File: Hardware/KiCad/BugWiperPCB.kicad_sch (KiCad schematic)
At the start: 0 parts

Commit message: update KiCAD files
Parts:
- added J2: Conn_01x06, symbol Connector_Generic:Conn_01x06
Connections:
- new net +3V3: J2.2 (Pin_2)
- new net EN_C1: J2.4 (Pin_4)
- new net EN_C2: J2.3 (Pin_3)
- new net GND: J2.5 (Pin_5)
- new net Motor+: J2.1 (Pin_1)
- new net Motor-: J2.6 (Pin_6)
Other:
- sheet ESP32-S3 ports: added ADC_VBat, Encoder_C1, Encoder_C2, M_IHN2, M_IN1, M_IN2, M_INH1, M_IS1, M_IS2; removed none
- sheet Power ports: added +3V3, +VBat, -VBat, ADC_VBat, GND, M_IN1, M_IN2, M_INH1, M_INH2, M_IS1, M_IS2, Motor+, Motor-; removed none
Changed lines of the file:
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@@
 (kicad_sch (version 20230121) (generator eeschema)
   (paper "A4")
-  (sheet (at 142.24 73.66) (size 33.02 21.59) (fields_autoplaced)
+  (wire (pts (xy 214.63 140.97) (xy 220.98 140.97))
+    (stroke (width 0) (type default))
+  )
+  (wire (pts (xy 180.34 73.66) (xy 187.96 73.66))
+    (stroke (width 0) (type default))
+  )
+  (wire (pts (xy 116.84 76.2) (xy 142.24 76.2))
+    (stroke (width 0) (type default))
+  )
+  (wire (pts (xy 214.63 138.43) (xy 220.98 138.43))
+    (stroke (width 0) (type default))
+  )
+  (wire (pts (xy 116.84 64.77) (xy 142.24 64.77))
+    (stroke (width 0) (type default))
+  )
+  (wire (pts (xy 214.63 143.51) (xy 220.98 143.51))
+    (stroke (width 0) (type default))
+  )
+  (wire (pts (xy 180.34 80.01) (xy 187.96 80.01))
+    (stroke (width 0) (type default))
+  )
+  (wire (pts (xy 214.63 151.13) (xy 220.98 151.13))
+    (stroke (width 0) (type default))
+  )
+  (wire (pts (xy 116.84 54.61) (xy 142.24 54.61))
+    (stroke (width 0) (type default))
+  )
+  (wire (pts (xy 72.39 74.93) (xy 76.2 74.93))
+    (stroke (width 0) (type default))
+  )
+  (wire (pts (xy 214.63 148.59) (xy 220.98 148.59))
+    (stroke (width 0) (type default))
+  )
+  (wire (pts (xy 116.84 99.06) (xy 142.24 99.06))
+    (stroke (width 0) (type default))
+  )
+  (wire (pts (xy 116.84 73.66) (xy 142.24 73.66))
+    (stroke (width 0) (type default))
+  )
+  (wire (pts (xy 116.84 50.8) (xy 142.24 50.8))
+    (stroke (width 0) (type default))
+  )
+  (wire (pts (xy 72.39 71.12) (xy 76.2 71.12))
+    (stroke (width 0) (type default))
+  )
+  (wire (pts (xy 214.63 146.05) (xy 220.98 146.05))
+    (stroke (width 0) (type default))
+  )
+  (wire (pts (xy 116.84 67.31) (xy 142.24 67.31))
+    (stroke (width 0) (type default))
+  )
+  (global_label "EN_C1" (shape input) (at 214.63 146.05 180) (fields_autoplaced)
+    (effects (font (size 1.27 1.27)) (justify right))
+    (property "Intersheetrefs" "${INTERSHEET_REFS}" (at 205.7182 146.05 0)
+      (effects (font (size 1.27 1.27)) (justify right) hide)
+    )
+  )
+  (global_label "Motor-" (shape input) (at 214.63 151.13 180) (fields_autoplaced)
+    (effects (font (size 1.27 1.27)) (justify right))
+    (property "Intersheetrefs" "${INTERSHEET_REFS}" (at 204.8111 151.13 0)
+      (effects (font (size 1.27 1.27)) (justify right) hide)
+    )
+  )
+  (global_label "+3V3" (shape input) (at 214.63 140.97 180) (fields_autoplaced)
+    (effects (font (size 1.27 1.27)) (justify right))
+    (property "Intersheetrefs" "${INTERSHEET_REFS}" (at 206.5648 140.97 0)
+      (effects (font (size 1.27 1.27)) (justify right) hide)
+    )
+  )
+  (global_label "Motor+" (shape input) (at 214.63 138.43 180) (fields_autoplaced)
+    (effects (font (size 1.27 1.27)) (justify right))
+    (property "Intersheetrefs" "${INTERSHEET_REFS}" (at 204.8111 138.43 0)
+      (effects (font (size 1.27 1.27)) (justify right) hide)
+    )
+  )
+  (global_label "GND" (shape input) (at 214.63 148.59 180) (fields_autoplaced)
+    (effects (font (size 1.27 1.27)) (justify right))
+    (property "Intersheetrefs" "${INTERSHEET_REFS}" (at 207.7743 148.59 0)
+      (effects (font (size 1.27 1.27)) (justify right) hide)
+    )
+  )
+  (global_label "Motor+" (shape input) (at 187.96 73.66 0) (fields_autoplaced)
+    (effects (font (size 1.27 1.27)) (justify left))
+    (property "Intersheetrefs" "${INTERSHEET_REFS}" (at 197.7789 73.66 0)
+      (effects (font (size 1.27 1.27)) (justify left) hide)
+    )
+  )
+  (global_label "Motor-" (shape input) (at 187.96 80.01 0) (fields_autoplaced)
+    (effects (font (size 1.27 1.27)) (justify left))
+    (property "Intersheetrefs" "${INTERSHEET_REFS}" (at 197.7789 80.01 0)
+      (effects (font (size 1.27 1.27)) (justify left) hide)
+    )
+  )
+  (global_label "EN_C2" (shape input) (at 72.39 74.93 180) (fields_autoplaced)
+    (effects (font (size 1.27 1.27)) (justify right))
+    (property "Intersheetrefs" "${INTERSHEET_REFS}" (at 63.4782 74.93 0)
+      (effects (font (size 1.27 1.27)) (justify right) hide)
+    )
+  )
+  (global_label "EN_C2" (shape input) (at 214.63 143.51 180) (fields_autoplaced)
+    (effects (font (size 1.27 1.27)) (justify right))
+    (property "Intersheetrefs" "${INTERSHEET_REFS}" (at 205.7182 143.51 0)
+      (effects (font (size 1.27 1.27)) (justify right) hide)
+    )
+  )
+  (global_label "EN_C1" (shape input) (at 72.39 71.12 180) (fields_autoplaced)
+    (effects (font (size 1.27 1.27)) (justify right))
+    (property "Intersheetrefs" "${INTERSHEET_REFS}" (at 63.4782 71.12 0)
+      (effects (font (size 1.27 1.27)) (justify right) hide)
+    )
+  )
+  (symbol (lib_id "Connector_Generic:Conn_01x06") (at 226.06 143.51 0) (unit 1)
+    (in_bom yes) (on_board yes) (dnp no) (fields_autoplaced)
+    (property "Reference" "J2" (at 228.6 143.51 0)
+      (effects (font (size 1.27 1.27)) (justify left))
+    )
+    (property "Value" "Conn_01x06" (at 228.6 146.05 0)
+      (effects (font (size 1.27 1.27)) (justify left))
+    )
+    (property "Footprint" "" (at 226.06 143.51 0)
+      (effects (font (size 1.27 1.27)) hide)
+    )
+    (property "Datasheet" "~" (at 226.06 143.51 0)
+      (effects (font (size 1.27 1.27)) hide)
+    )
+    (pin "2")
+    (pin "1")
+    (pin "6")
+    (pin "4")
+    (pin "5")
+    (pin "3")
+    (instances
+      (project "BugWiperPCB"
+        (path "/d31a15bd-db02-4d4c-9593-17c596d3182c"
+          (reference "J2") (unit 1)
+        )
+      )
+    )
+  )
+  (sheet (at 142.24 46.99) (size 38.1 57.15) (fields_autoplaced)
     (stroke (width 0.1524) (type solid))
     (fill (color 0 0 0 0.0000))
-    (property "Sheetname" "Power" (at 142.24 72.9484 0)
+    (property "Sheetname" "Power" (at 142.24 46.2784 0)
       (effects (font (size 1.27 1.27)) (justify left bottom))
     )
-    (property "Sheetfile" "Power.kicad_sch" (at 142.24 95.8346 0)
+    (property "Sheetfile" "Power.kicad_sch" (at 142.24 104.7246 0)
       (effects (font (size 1.27 1.27)) (justify left top))
+    )
+    (pin "+VBat" input (at 153.67 46.99 90)
+      (effects (font (size 1.27 1.27)) (justify right))
+    )
+    (pin "Motor+" input (at 180.34 73.66 0)
+      (effects (font (size 1.27 1.27)) (justify right))
+    )
+    (pin "Motor-" input (at 180.34 80.01 0)
+      (effects (font (size 1.27 1.27)) (justify right))
+    )
+    (pin "ADC_VBat" input (at 142.24 99.06 180)
+      (effects (font (size 1.27 1.27)) (justify left))
+    )
+    (pin "-VBat" input (at 160.02 46.99 90)
+      (effects (font (size 1.27 1.27)) (justify right))
+    )
+    (pin "M_IN1" input (at 142.24 64.77 180)
+      (effects (font (size 1.27 1.27)) (justify left))
+    )
+    (pin "M_IS2" input (at 142.24 95.25 180)
+      (effects (font (size 1.27 1.27)) (justify left))
+    )
+    (pin "M_IS1" input (at 142.24 91.44 180)
+      (effects (font (size 1.27 1.27)) (justify left))
+    )
+    (pin "M_IN2" input (at 142.24 67.31 180)
+      (effects (font (size 1.27 1.27)) (justify left))
+    )
+    (pin "M_INH2" input (at 142.24 76.2 180)
+      (effects (font (size 1.27 1.27)) (justify left))
+    )
+    (pin "M_INH1" input (at 142.24 73.66 180)
+      (effects (font (size 1.27 1.27)) (justify left))
+    )
+    (pin "+3V3" input (at 142.24 50.8 180)
+      (effects (font (size 1.27 1.27)) (justify left))
+    )
+    (pin "GND" input (at 142.24 54.61 180)
+      (effects (font (size 1.27 1.27)) (justify left))
     )
     (instances
@@
     )
   )
-  (sheet (at 86.36 64.77) (size 29.21 40.64) (fields_autoplaced)
+  (sheet (at 76.2 46.99) (size 40.64 57.15) (fields_autoplaced)
     (stroke (width 0.1524) (type solid))
-    (fill (color 0 0 0 0.0000))
-    (property "Sheetname" "ESP32-S3" (at 86.36 64.0584 0)
+    (fill (color 0 194 0 0.5400))
+    (property "Sheetname" "ESP32-S3" (at 76.2 46.2784 0)
       (effects (font (size 1.27 1.27)) (justify left bottom))
     )
-    (property "Sheetfile" "ESP32-S3.kicad_sch" (at 86.36 105.9946 0)
+    (property "Sheetfile" "ESP32-S3.kicad_sch" (at 76.2 104.7246 0)
       (effects (font (size 1.27 1.27)) (justify left top))
     )
-    (pin "+3V3" input (at 115.57 68.58 0)
-      (effects (font (size 1.27 1.27)) (justify right))
-    )
-    (pin "GND" input (at 115.57 82.55 0)
-      (effects (font (size 1.27 1.27)) (justify right))
-    )
+    (pin "+3V3" input (at 116.84 50.8 0)
+      (effects (font (size 1.27 1.27)) (justify right))
+    )
+    (pin "GND" input (at 116.84 54.61 0)
+      (effects (font (size 1.27 1.27)) (justify right))
+    )
+    (pin "Encoder_C1" input (at 76.2 71.12 180)
+      (effects (font (size 1.27 1.27)) (justify left))
+    )
+    (pin "Encoder_C2" input (at 76.2 74.93 180)
+      (effects (font (size 1.27 1.27)) (justify left))
+    )
+    (pin "ADC_VBat" input (at 116.84 99.06 0)
+      (effects (font (size 1.27 1.27)) (justify right))
+    )
+    (pin "M_IS2" input (at 116.84 95.25 0)
+      (effects (font (size 1.27 1.27)) (justify right))
+    )
+    (pin "M_IS1" input (at 116.84 91.44 0)
+      (effects (font (size 1.27 1.27)) (justify right))
+    )
+    (pin "M_IN1" input (at 116.84 64.77 0)
+      (effects (font (size 1.27 1.27)) (justify right))
+    )
+    (pin "M_IN2" input (at 116.84 67.31 0)
+      (effects (font (size 1.27 1.27)) (justify right))
+    )
+    (pin "M_INH1" input (at 116.84 73.66 0)
+      (effects (font (size 1.27 1.27)) (justify right))
+    )
+    (pin "M_IHN2" input (at 116.84 76.2 0)
+      (effects (font (size 1.27 1.27)) (justify right))
+    )

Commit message: Update PCB
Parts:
- removed J2: Conn_01x06, symbol Connector_Generic:Conn_01x06
- added H1, H2, H3, H4, H5: MountingHole, MountingHole:MountingHole_3.2mm_M3_DIN965, symbol Mechanical:MountingHole
- added H6: MountingHole_Pad, MountingHole:MountingHole_3.2mm_M3_DIN965_Pad_TopBottom, symbol Mechanical:MountingHole_Pad
- added J2: TBLH10-350-06BK, TBLH10_350_06BK-2:CUI_TBLH10-350-06BK, symbol TBLH10-350-06BK:TBLH10-350-06BK
- added J3: Phoenix_1776508, BugWiper_lib:PHOENIX_1776508, symbol BugWiper_Lib:Phoenix_1776508
- added R27: R, symbol Device:R
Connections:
- net +3V3: now also J2.3_A (3), J2.3_B (3__1)
- net EN_C1: now also J2.6_B (6__1)
- net EN_C2: now also J2.5_B (5__1)
- net GND: now also J2.4_A (4), J2.4_B (4__1), R27.2
- net Motor+: now also J2.1_A (1), J2.1_B (1__1)
- net Motor-: now also J2.2_A (2), J2.2_B (2__1)
- net Power/+VBat: now also J3.2
- net Power/-VBat: now also J3.1
- new net: H6.1, R27.1

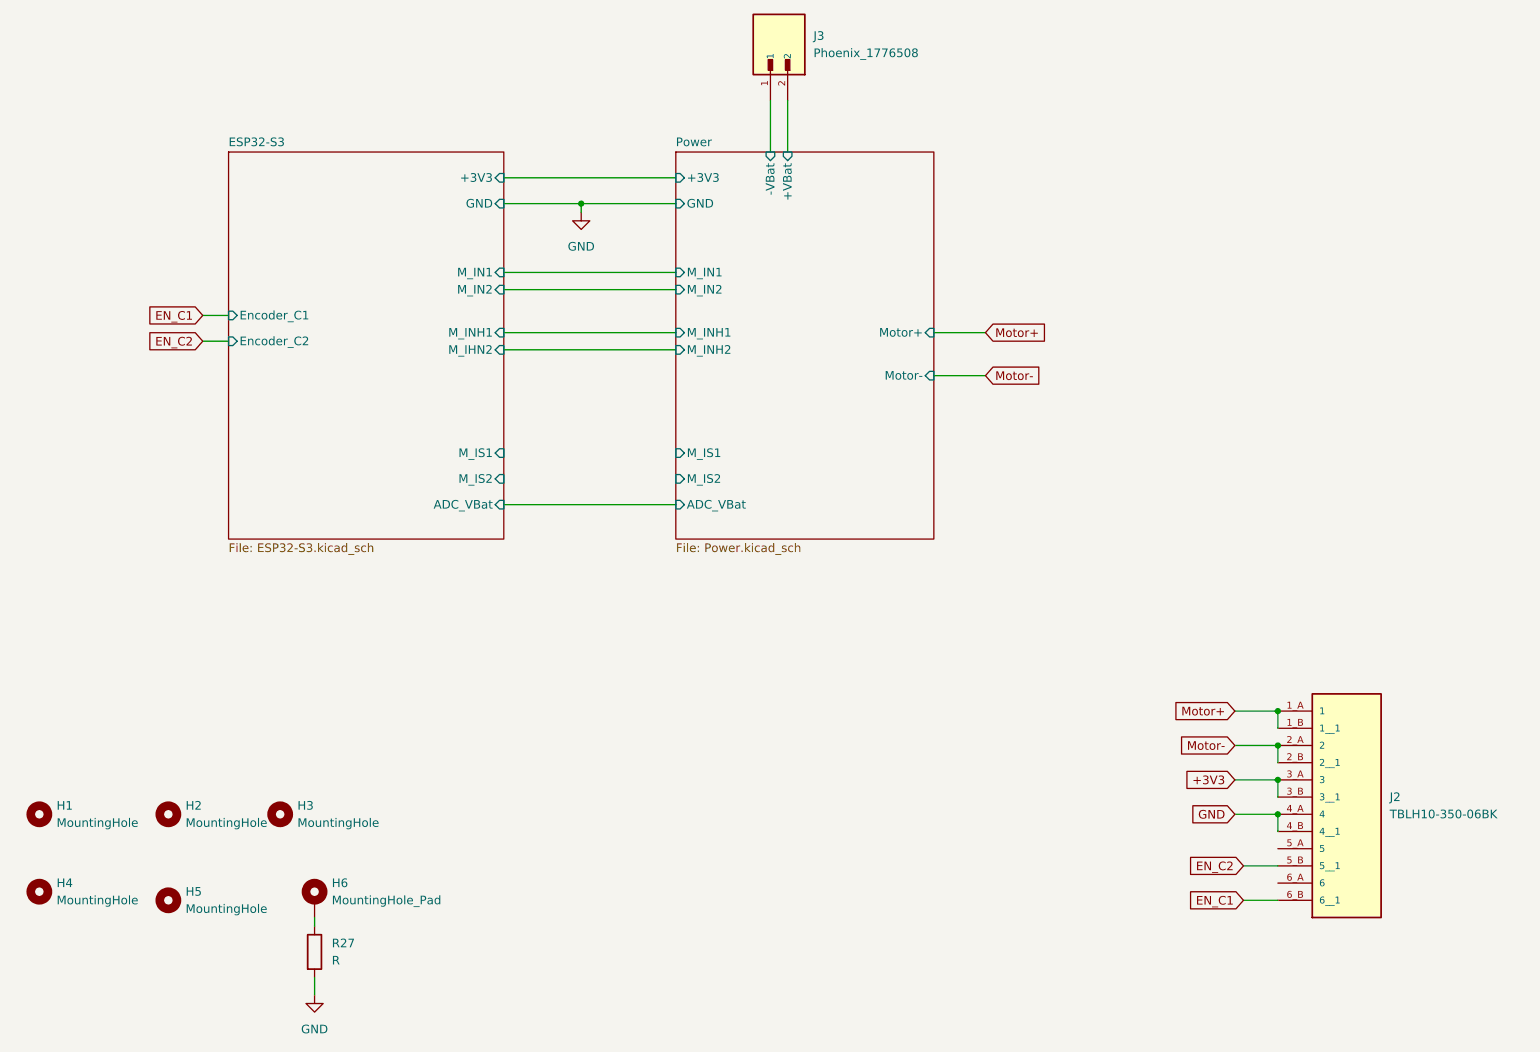
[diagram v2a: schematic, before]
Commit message: update PCB
add 12V to 3.3V converter and 5V to 3.3V for USB
add protections to the RJ45
component placement
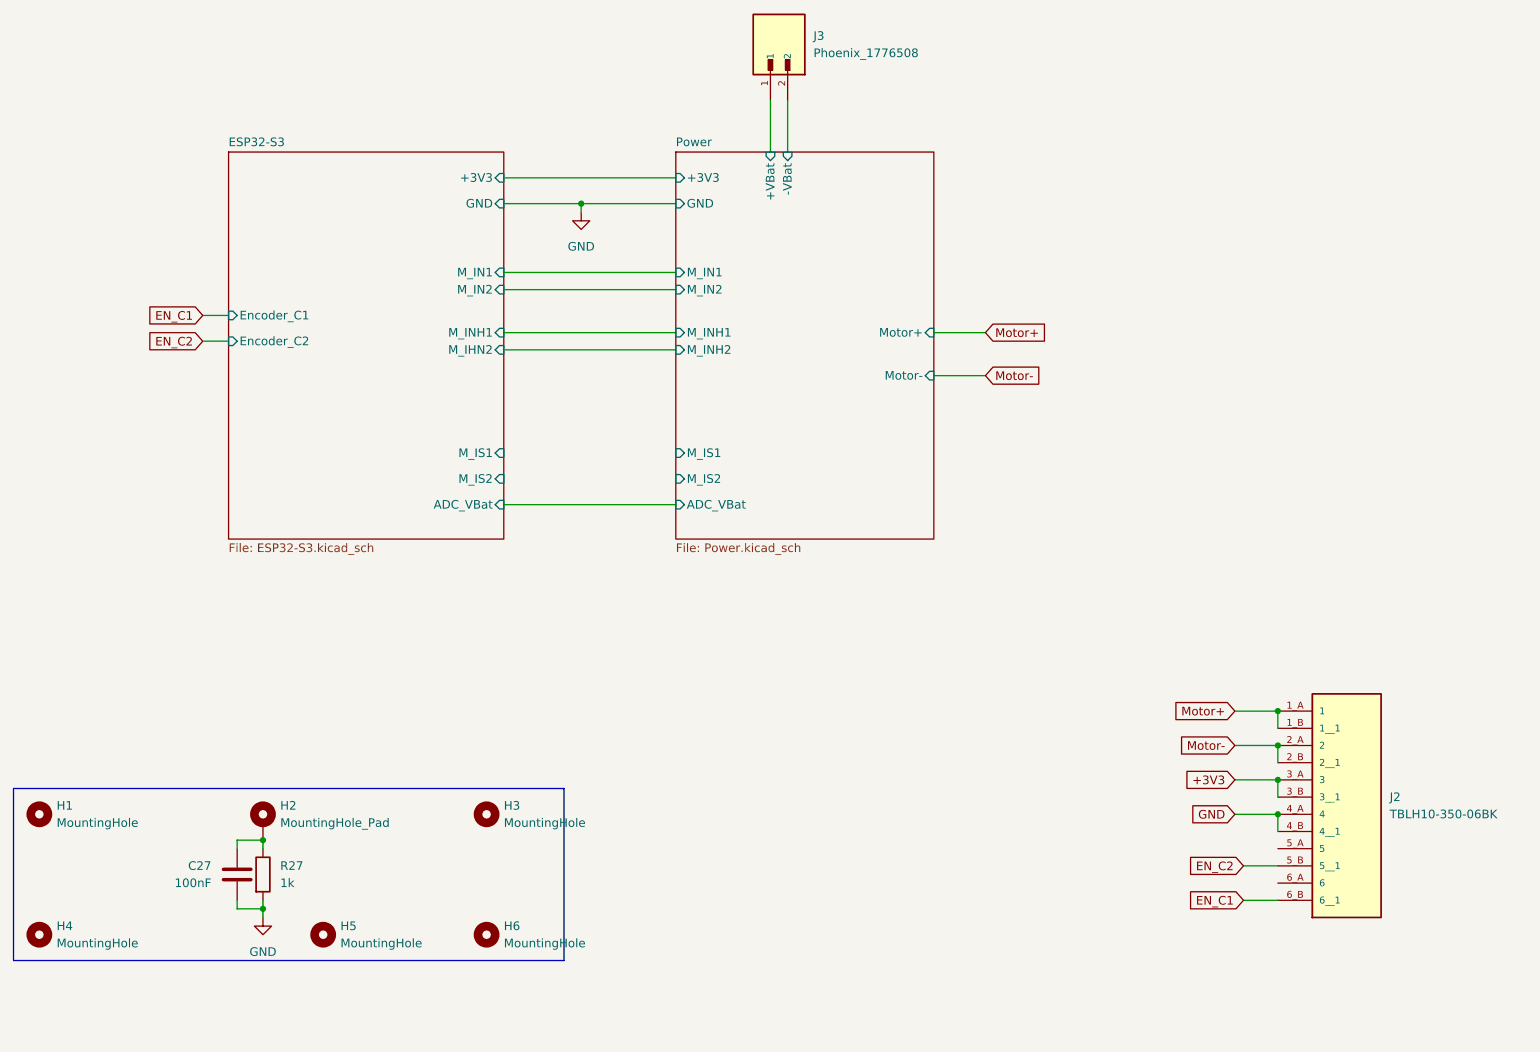
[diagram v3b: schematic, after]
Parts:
- added C27: 100nF, Capacitor_SMD:C_0603_1608Metric, symbol Device:C
- R27: value R -> 1k; footprint (none) -> Resistor_SMD:R_0603_1608Metric
- renumbered H6 to H2, H2 to H6
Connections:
- net GND: now also C27.2
- net Power/+VBat: now also J3.1; no longer J3.2
- net Power/-VBat: now also J3.2; no longer J3.1
- net at H2.1, R27.1: now also C27.1
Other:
- moved on the sheet: H2, H3, H4, H5, H6, R27

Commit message: add ESD protection to inputs
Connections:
- net EN_C1: now also J2.6_A (6)
- net EN_C2: now also J2.5_A (5)
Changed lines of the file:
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@@
   (junction (at 231.14 134.62) (diameter 0) (color 0 0 0 0)
+  )
+  (junction (at 231.14 157.48) (diameter 0) (color 0 0 0 0)
   )
   (junction (at 128.27 54.61) (diameter 0) (color 0 0 0 0)
@@
   (junction (at 231.14 129.54) (diameter 0) (color 0 0 0 0)
   )
+  (junction (at 231.14 152.4) (diameter 0) (color 0 0 0 0)
+  )
   (wire (pts (xy 226.06 152.4) (xy 231.14 152.4))
+    (stroke (width 0) (type default))
+  )
+  (wire (pts (xy 231.14 154.94) (xy 231.14 157.48))
     (stroke (width 0) (type default))
   )
@@
     (stroke (width 0) (type default))
   )
+  (wire (pts (xy 231.14 149.86) (xy 231.14 152.4))
+    (stroke (width 0) (type default))
+  )
